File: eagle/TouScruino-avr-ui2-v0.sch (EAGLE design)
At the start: 60 parts, among them J1 AVR_ISP, Q1 8MHz, Q2 MMBT2222A, Q3 8MHz, U1 ATMEGA1284P, U2 AR1021, U3 MIC5209-3.3YS, U4 MCP73831, X2 USB

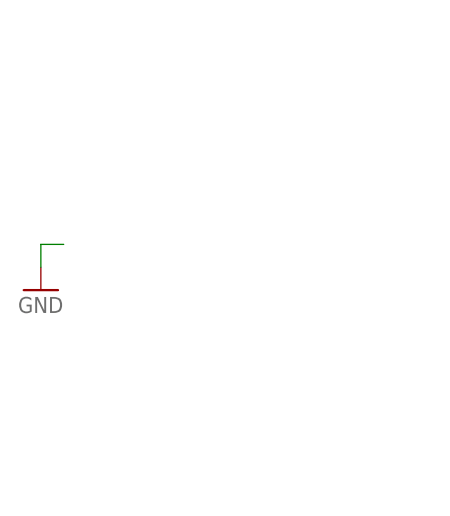
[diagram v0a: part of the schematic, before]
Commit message: 
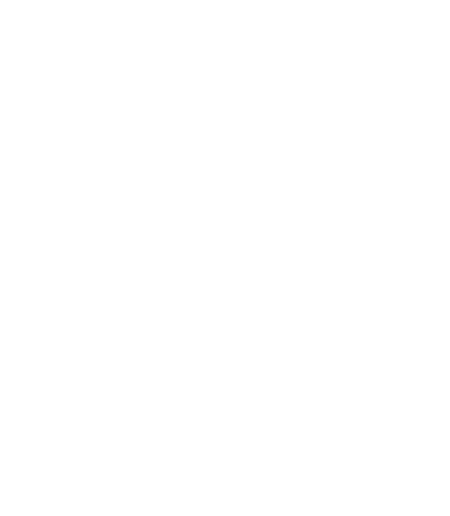
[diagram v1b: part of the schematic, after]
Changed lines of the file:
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@@
 <part name="LED2" library="wibauxl" deviceset="LED" device="" value="Red"/>
 <part name="SJ6" library="SparkFun" deviceset="SOLDERJUMPER" device="TRACE" value=""/>
-<part name="GND31" library="supply1" deviceset="GND" device=""/>
 <part name="R11" library="SparkFun" deviceset="RESISTOR" device="0805-RES" value="10"/>
 <part name="R12" library="SparkFun" deviceset="RESISTOR" device="0805-RES" value="10"/>
@@
 <instance part="LED2" gate="G$1" x="154.94" y="165.1" rot="MR270"/>
 <instance part="SJ6" gate="1" x="215.9" y="109.22"/>
-<instance part="GND31" gate="1" x="-43.18" y="-175.26"/>
 <instance part="R11" gate="G$1" x="106.68" y="-160.02"/>
 <instance part="R12" gate="G$1" x="106.68" y="-167.64"/>
@@
 </segment>
 <segment>
-<wire x1="-40.64" y1="-170.18" x2="-43.18" y2="-170.18" width="0.1524" layer="91"/>
-<wire x1="-43.18" y1="-170.18" x2="-43.18" y2="-172.72" width="0.1524" layer="91"/>
-<pinref part="GND31" gate="1" pin="GND"/>
-</segment>
-<segment>

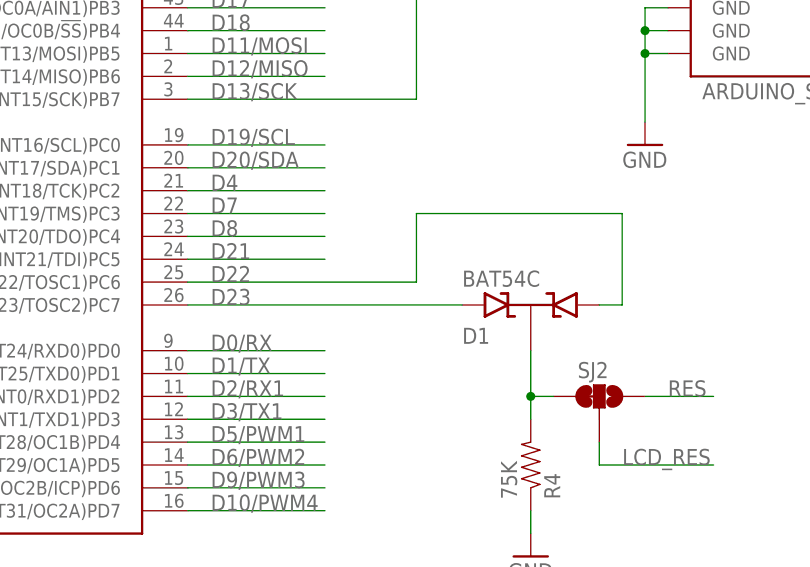
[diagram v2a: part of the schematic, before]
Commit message: 
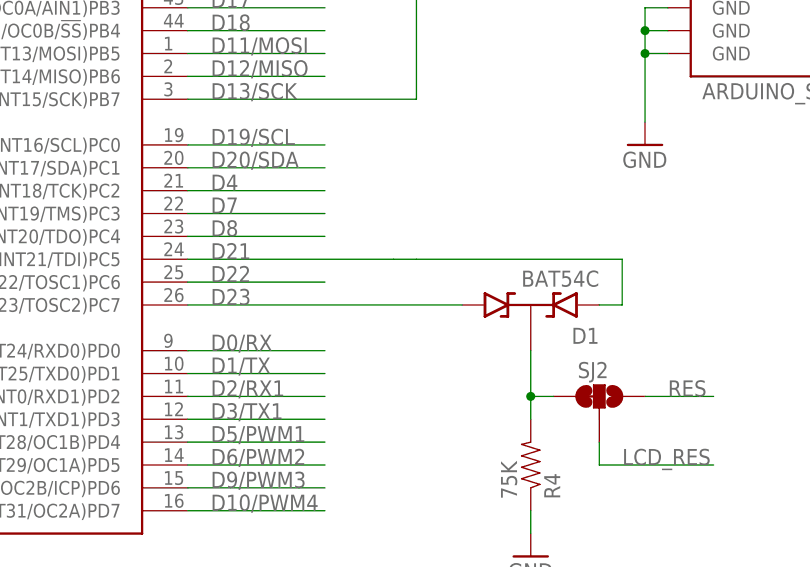
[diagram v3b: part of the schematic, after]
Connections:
- net D21: now also D1.A2
- net D22: no longer D1.A1
- net D23: now also D1.A1; no longer D1.A2
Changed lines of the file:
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@@
 <instance part="U$5" gate="G$1" x="231.14" y="-165.1"/>
 <instance part="JP4" gate="G$1" x="226.06" y="-96.52" rot="R180"/>
-<instance part="D1" gate="G$1" x="147.32" y="83.82" rot="MR180"/>
+<instance part="D1" gate="G$1" x="147.32" y="83.82" rot="R180"/>
 <instance part="R4" gate="G$1" x="147.32" y="66.04" rot="MR90"/>
 <instance part="GND18" gate="1" x="147.32" y="55.88"/>
@@
 <label x="111.76" y="83.82" size="1.778" layer="95"/>
 <pinref part="U1" gate="G$1" pin="(PCINT23/TOSC2)PC7"/>
-<pinref part="D1" gate="G$1" pin="A2"/>
 <wire x1="109.22" y1="83.82" x2="139.7" y2="83.82" width="0.1524" layer="91"/>
+<pinref part="D1" gate="G$1" pin="A1"/>
 </segment>
 <segment>
@@
 <net name="D22" class="0">
 <segment>
-<wire x1="109.22" y1="86.36" x2="134.62" y2="86.36" width="0.1524" layer="91"/>
-<wire x1="134.62" y1="86.36" x2="134.62" y2="93.98" width="0.1524" layer="91"/>
+<wire x1="109.22" y1="86.36" x2="124.46" y2="86.36" width="0.1524" layer="91"/>
 <label x="111.76" y="86.36" size="1.778" layer="95"/>
 <pinref part="U1" gate="G$1" pin="(PCINT22/TOSC1)PC6"/>
-<pinref part="D1" gate="G$1" pin="A1"/>
-<wire x1="134.62" y1="93.98" x2="157.48" y2="93.98" width="0.1524" layer="91"/>
-<wire x1="157.48" y1="93.98" x2="157.48" y2="83.82" width="0.1524" layer="91"/>
-<wire x1="157.48" y1="83.82" x2="154.94" y2="83.82" width="0.1524" layer="91"/>
 </segment>
 <segment>
@@
 <net name="D21" class="0">
 <segment>
-<wire x1="109.22" y1="88.9" x2="124.46" y2="88.9" width="0.1524" layer="91"/>
 <label x="111.76" y="88.9" size="1.778" layer="95"/>
 <pinref part="U1" gate="G$1" pin="(PCINT21/TDI)PC5"/>
-</segment>
-<segment>
+<wire x1="109.22" y1="88.9" x2="132.08" y2="88.9" width="0.1524" layer="91"/>
+<wire x1="132.08" y1="88.9" x2="134.62" y2="88.9" width="0.1524" layer="91"/>
+<wire x1="134.62" y1="88.9" x2="157.48" y2="88.9" width="0.1524" layer="91"/>
+<wire x1="157.48" y1="88.9" x2="157.48" y2="83.82" width="0.1524" layer="91"/>
+<pinref part="D1" gate="G$1" pin="A2"/>
+<wire x1="154.94" y1="83.82" x2="157.48" y2="83.82" width="0.1524" layer="91"/>
+</segment>
+<segment>
